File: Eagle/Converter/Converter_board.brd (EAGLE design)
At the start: 100 x 80 mm, 9 parts

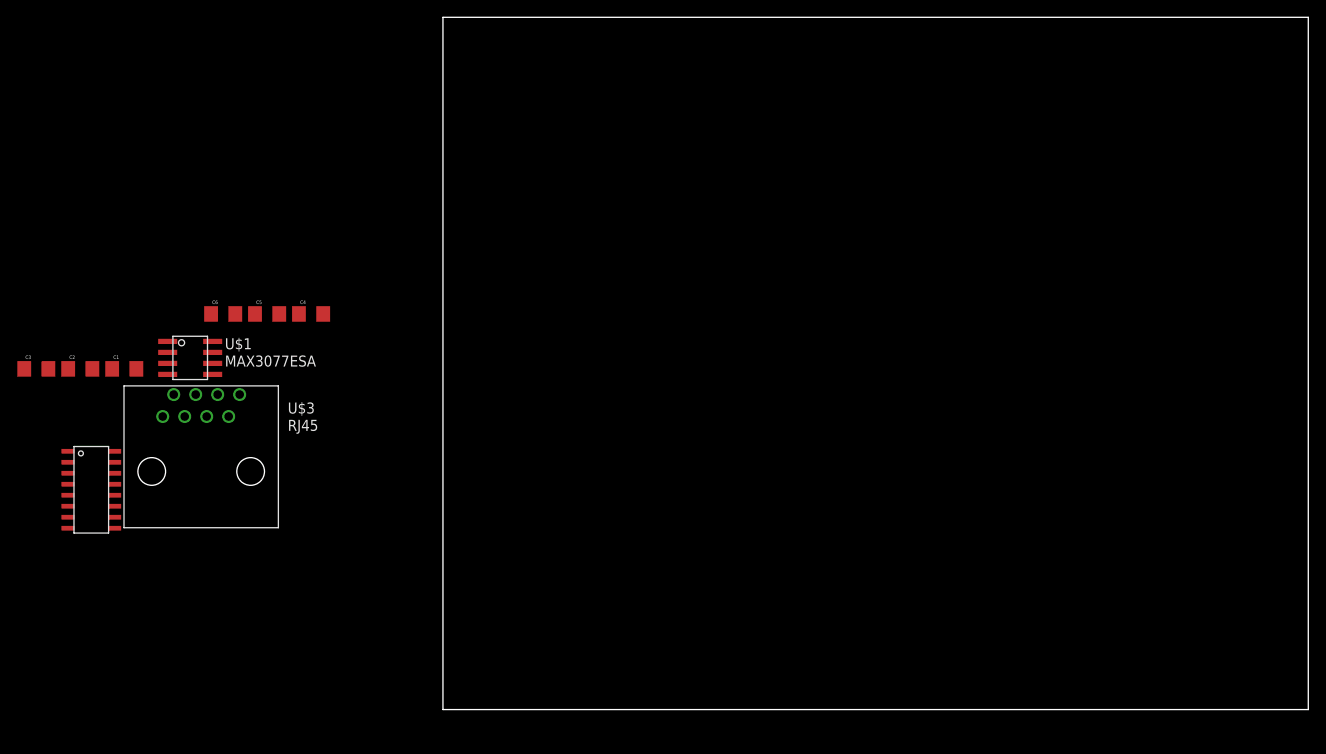
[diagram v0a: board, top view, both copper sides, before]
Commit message: Added all parts needed
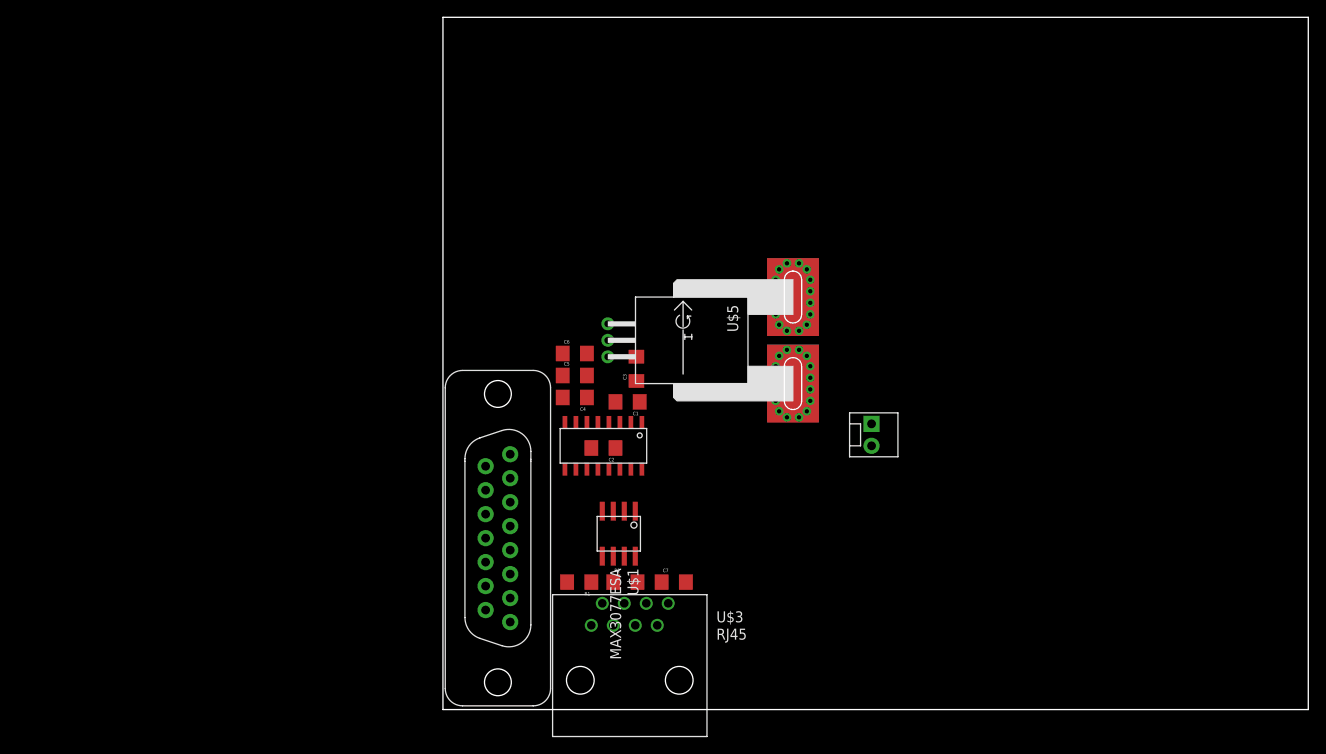
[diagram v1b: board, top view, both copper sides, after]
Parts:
- added C7: 0.1uF, SparkFun-Capacitors:1206
- added JP1: M02POLAR, SparkFun-Connectors:MOLEX-1X2
- added R1, R2: 120, SparkFun-Passives:1206
- added U$4: DB15, MRDT-LIB2014:DB15
- added U$5: ACS756, MRDT-2015-BMS:PFF_LEADFORM
- C1, C2, C3, C4, C5, C6: value (none) -> 0.1uF
- moved C3 69.3 mm to (22.4, 39.4), turned to 90 degrees
- moved C2 61.1 mm to (18.5, 30.2), turned to 180 degrees
- moved U$2 59.4 mm to (18.5, 30.5), turned to 270 degrees
- moved C1 58.3 mm to (21.3, 35.6), turned to 180 degrees
- moved U$3 55.1 mm to (21.6, 5.08)
- moved U$1 53.5 mm to (20.3, 20.3), turned to 270 degrees
- moved C6 40.9 mm to (15.2, 41.1)
- moved C5 36.3 mm to (15.2, 38.6)
- moved C4 32.0 mm to (15.2, 36.1), turned to 180 degrees
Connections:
- new net ANA1: U$4.4, U$5.3
- new net N$7: JP1.2, U$5.4_1, U$5.4_10, U$5.4_11, U$5.4_12, U$5.4_13, U$5.4_14, U$5.4_15, U$5.4_16, U$5.4_2, U$5.4_3, U$5.4_4, U$5.4_5, U$5.4_6, U$5.4_7, U$5.4_8, U$5.4_9, U$5.4_B, U$5.4_T
- new net N$9: JP1.1, U$5.5_1, U$5.5_10, U$5.5_11, U$5.5_12, U$5.5_13, U$5.5_14, U$5.5_15, U$5.5_16, U$5.5_2, U$5.5_3, U$5.5_4, U$5.5_5, U$5.5_6, U$5.5_7, U$5.5_8, U$5.5_9, U$5.5_B, U$5.5_T
- net GND: now also C7.2, U$4.13, U$4.5, U$5.2
- net REC+: now also R2.2, U$1.5; no longer U$1.7
- net REC-: now also R2.1, U$1.6; no longer U$1.8
- net R_OUT1: now also U$4.3
- net TRANS+: now also R1.2, U$1.7; no longer U$1.5
- net TRANS-: now also R1.1, U$1.8; no longer U$1.6
- net T_IN1: now also U$4.2; no longer U$1.3
- net T_OUT1: now also U$1.3
- net VCC: now also C7.1, U$4.14, U$5.1

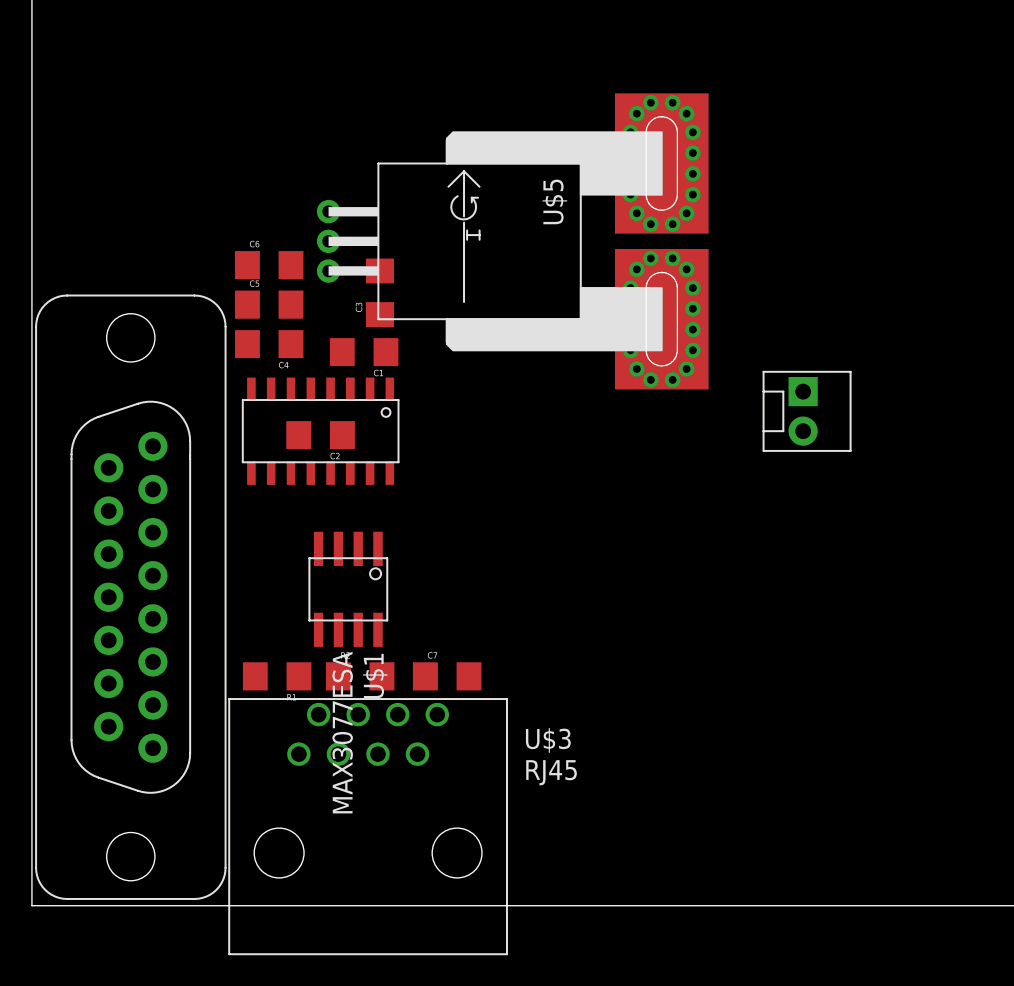
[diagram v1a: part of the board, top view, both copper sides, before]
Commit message: Finished Schematic, Setup Board Layout. Waiting to hear final decision on Torque control.
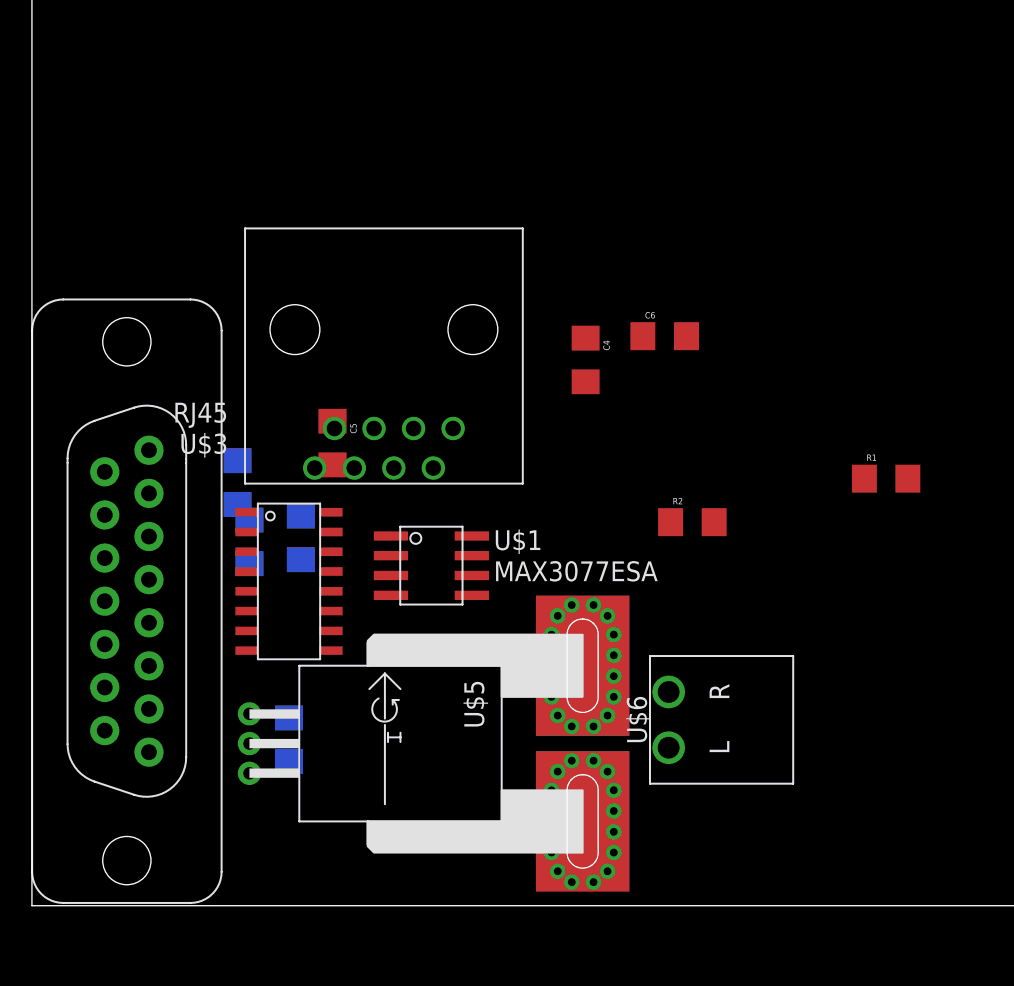
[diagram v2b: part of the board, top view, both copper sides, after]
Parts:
- removed JP1: M02POLAR, SparkFun-Connectors:MOLEX-1X2
- added U$6: H_WR-TBL_321*0002HORIZ, MRDT-2015-PowerBoard:691322110002
- moved R1 41.1 mm to (54.9, 27.4), turned to 0 degrees
- moved U$5 32.7 mm to (14.0, 10.4)
- moved U$3 30.2 mm to (22.6, 35.3), turned to 180 degrees
- moved C6 25.8 mm to (40.6, 36.6)
- moved R2 23.5 mm to (42.4, 24.6)
- moved C4 20.3 mm to (35.6, 35.1), turned to 270 degrees
- moved C3 16.5 mm to (17.3, 23.6), flipped to the bottom
- moved C1 11.7 mm to (13.2, 27.2), flipped to the bottom, turned to 270 degrees
- moved C7 10.9 mm to (16.5, 10.7), flipped to the bottom, turned to 270 degrees
- moved U$2 9.86 mm to (16.5, 20.8), turned to 0 degrees
- moved C5 9.77 mm to (19.3, 29.7), turned to 270 degrees
- moved C2 8.24 mm to (14.0, 23.4), flipped to the bottom, turned to 270 degrees
- moved U$1 5.55 mm to (25.7, 21.8), turned to 0 degrees
- moved U$4 0.36 mm to (6.10, 19.6)
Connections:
- removed net N$9: JP1.1, U$5.5_1, U$5.5_10, U$5.5_11, U$5.5_12, U$5.5_13, U$5.5_14, U$5.5_15, U$5.5_16, U$5.5_2, U$5.5_3, U$5.5_4, U$5.5_5, U$5.5_6, U$5.5_7, U$5.5_8, U$5.5_9, U$5.5_B, U$5.5_T
- new net N$8: U$5.5_1, U$5.5_10, U$5.5_11, U$5.5_12, U$5.5_13, U$5.5_14, U$5.5_15, U$5.5_16, U$5.5_2, U$5.5_3, U$5.5_4, U$5.5_5, U$5.5_6, U$5.5_7, U$5.5_8, U$5.5_9, U$5.5_B, U$5.5_T, U$6.R
- net N$7: now also U$6.L; no longer JP1.2
